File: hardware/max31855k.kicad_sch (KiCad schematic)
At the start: 9 parts, among them J5 Screw_Terminal_01x02, J6 Screw_Terminal_01x02, U2 MAX31855KASA

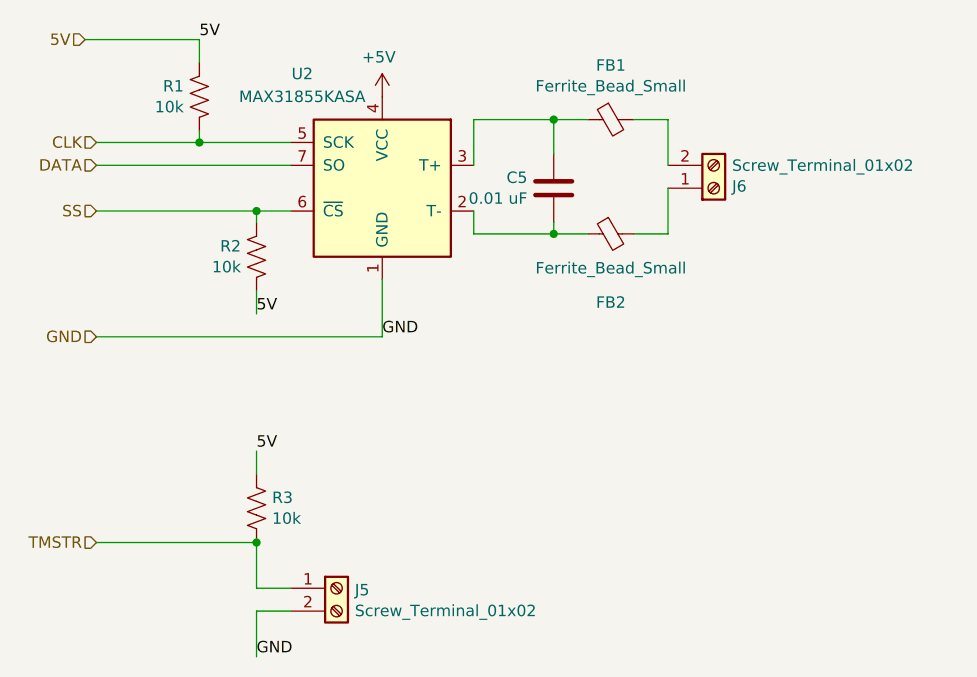
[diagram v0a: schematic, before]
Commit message: updated to the correct terminals and proper hierarchial pages
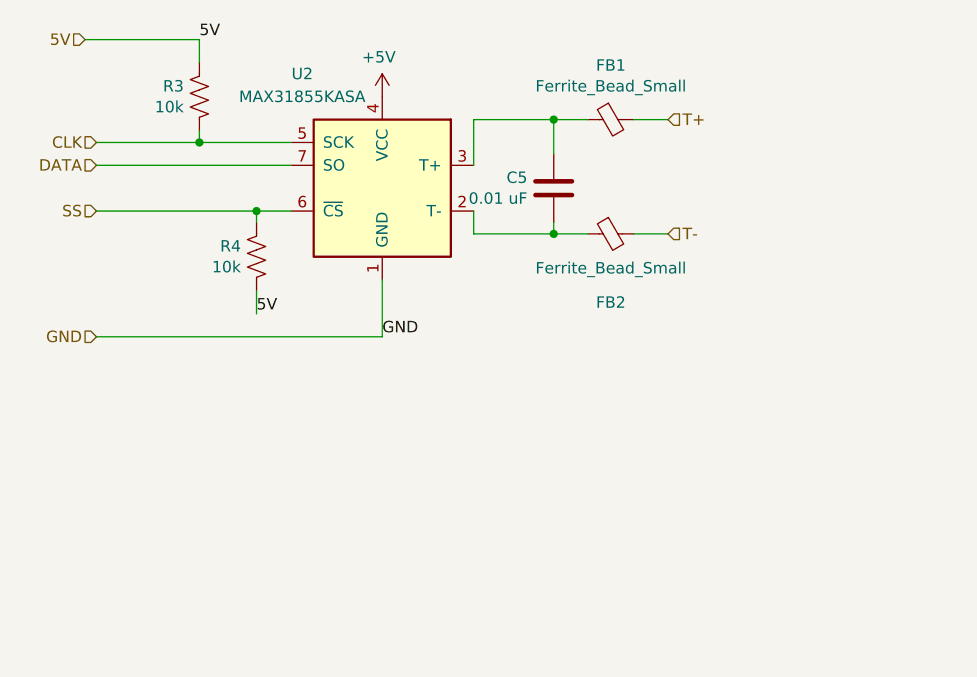
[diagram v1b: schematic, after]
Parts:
- removed J5, J6: Screw_Terminal_01x02, TerminalBlock_Phoenix:TerminalBlock_Phoenix_MKDS-1,5-2_1x02_P5.00mm_Horizontal, symbol Connector:Screw_Terminal_01x02
- removed R3: 10k, Resistor_SMD:R_1206_3216Metric_Pad1.30x1.75mm_HandSolder, symbol Device:R_US
- renumbered R1 to R3, R2 to R4
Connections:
- net T-: now reaches FB2.2
- net T+: now reaches FB1.2
